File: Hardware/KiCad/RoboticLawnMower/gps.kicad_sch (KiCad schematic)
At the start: 1 part, among them J9 GPS

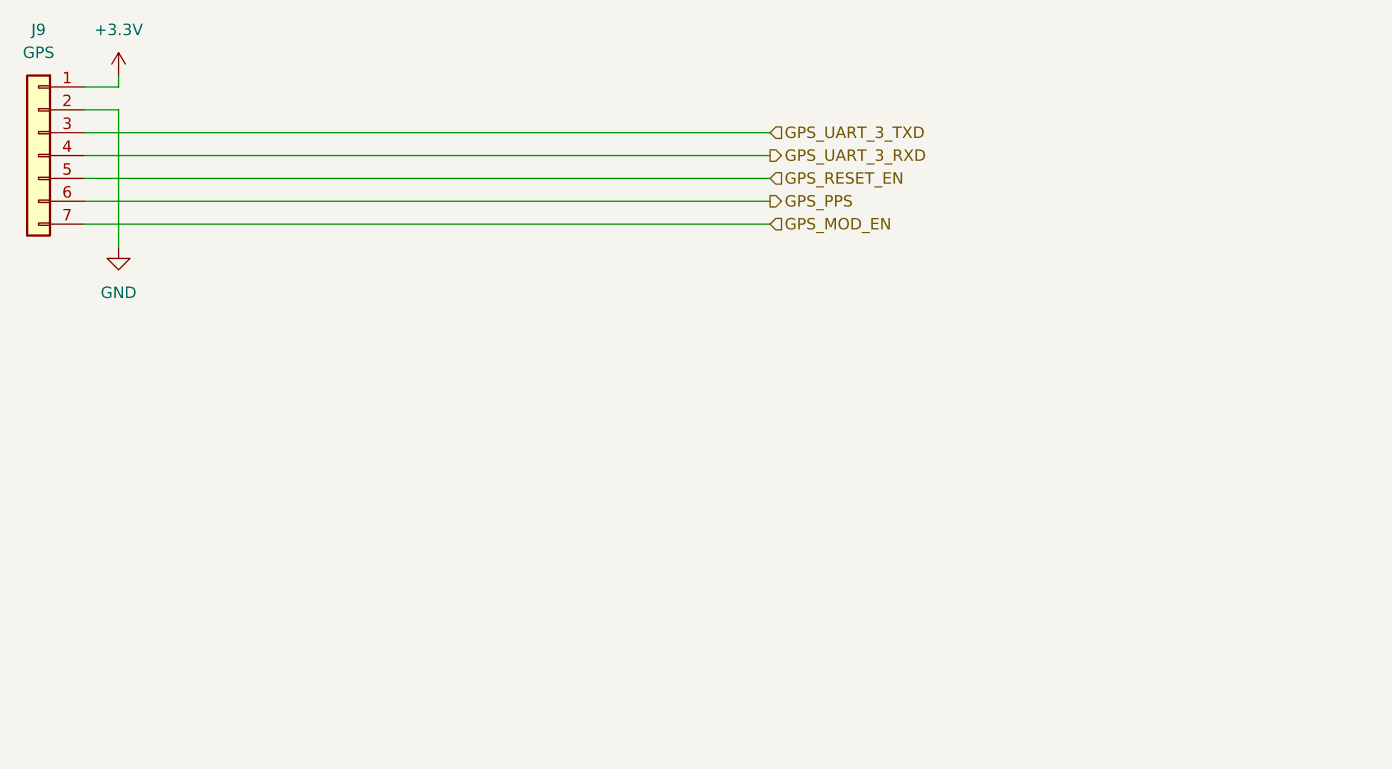
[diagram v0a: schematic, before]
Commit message: Redesign: - Controller - I2C pinning geändert - uvm
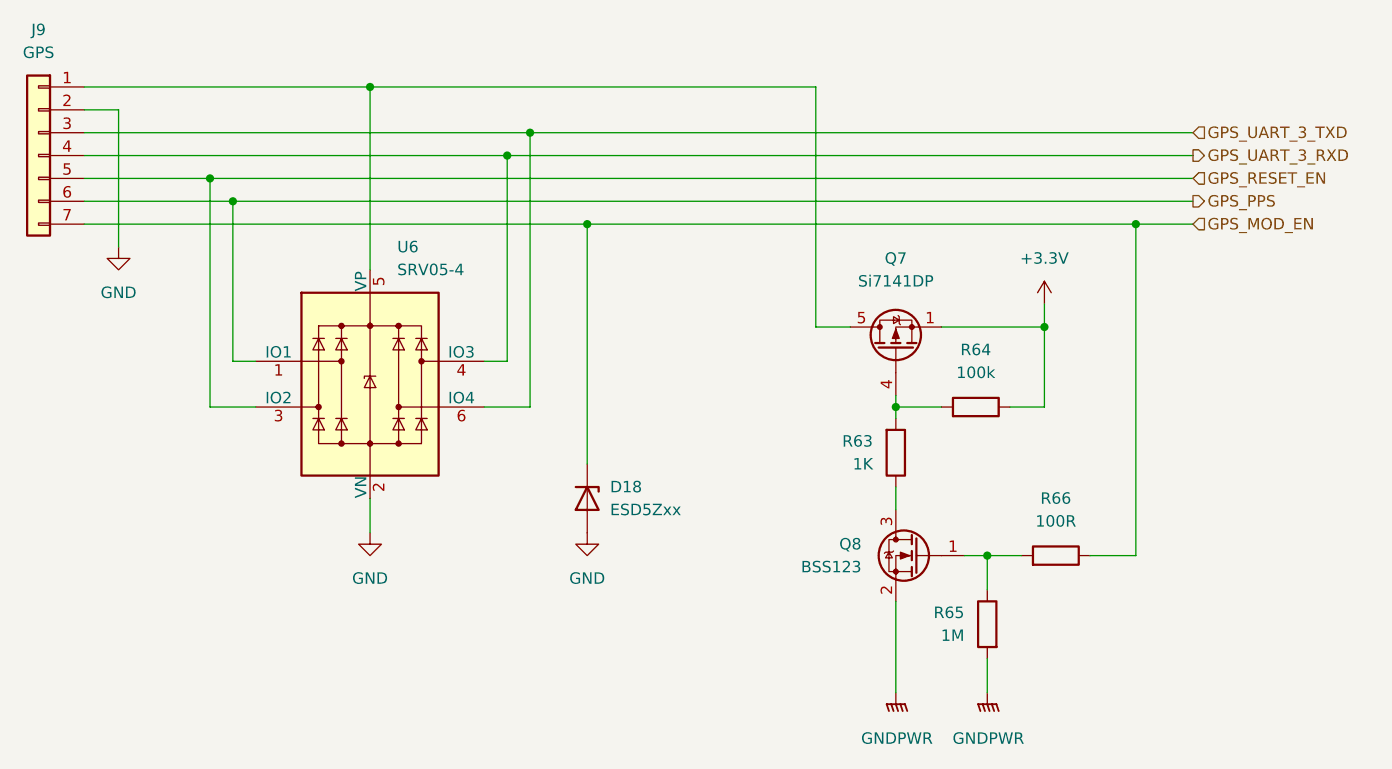
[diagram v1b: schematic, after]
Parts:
- added D18: ESD5Zxx, Diode_SMD:D_SOD-523, symbol Diode:ESD5Zxx
- added Q7: Si7141DP, Package_SO:PowerPAK_SO-8_Single, symbol Transistor_FET:Si7141DP
- added Q8: BSS123, Package_TO_SOT_SMD:SOT-23, symbol Transistor_FET:BSS123
- added R63: 1K, Resistor_SMD:R_0603_1608Metric, symbol Device:R
- added R64: 100k, Resistor_SMD:R_0603_1608Metric, symbol Device:R
- added R65: 1M, Resistor_SMD:R_0603_1608Metric, symbol Device:R
- added R66: 100R, Resistor_SMD:R_0603_1608Metric, symbol Device:R
- added U6: SRV05-4, Package_TO_SOT_SMD:SOT-23-6, symbol Power_Protection:SRV05-4
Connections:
- net +3.3V: now also Q7.1 (S), Q7.2 (S), Q7.3 (S), R64.1; no longer J9.1 (Pin_1)
- net GND: now also D18.2 (A), U6.2 (VN)
- net GPS_MOD_EN: now also D18.1 (K), R66.1
- net GPS_PPS: now also U6.1 (IO1)
- net GPS_RESET_EN: now also U6.3 (IO2)
- net GPS_UART_3_RXD: now also U6.4 (IO3)
- net GPS_UART_3_TXD: now also U6.6 (IO4)
- new net: Q8.3 (D), R63.1
- new net: Q7.4 (G), R63.2, R64.2
- new net: Q8.1 (G), R65.1, R66.2
- new net: J9.1 (Pin_1), Q7.5 (D), U6.5 (VP)
- new net GNDPWR: Q8.2 (S), R65.2
